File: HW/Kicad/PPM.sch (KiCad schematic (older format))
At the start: 400 parts, among them J1 12V, J10 hole, J11 hole, J12 hole, J13 hole, J14 External GPIOs, J15 External GPIOs, J16 External GPIOs, J17 C ext, J18 TP, J19 Shield pad, J2 PPM_sensor, J20 TP, J21 Shield pad, J22 TP, J23 Shield pad, J24 Shield pad, J25 Shield pad, J26 Shield pad, J27 Shield pad, J28 Shield pad, J29 Shield pad, J3 RS232, J30 Shield pad, J4 USB_B, J5 UART5, J6 SWD, J7 External GPIOs, J8 UART1, J9 Batt, Q1 DMPH4015SSSQ-13, Q10 IRF740, Q11 BC847, Q12 BC847, Q13 BC847, Q14 BC847, Q15 BC847, Q16 BC847, Q17 BC847, Q18 BC847, Q2 ZTX851, Q3 ZTX851, Q4 IRF9640, Q5 BC847, Q6 IRF740, Q7 IRF740, Q8 IRF640, Q9 IRF740, T1 Filter, T2 78253_55JC, U1 TPS7A4700, U10 LT1677, U11 STM32F767VITx, U12 LT1677, U13 MAX6043, U14 MAX11100, U15 ADCMP609, U16 LTC6655, U17 LT1677, U18 MCP1501-30E_SN, U19 LT1677, U2 LT1677, U20 MCP6021, U21 SN74ACT244-Q1, U22 MAX3227EE, U23 FT230XS, U24 ADuM226N, U25 SN6505, U3 ADA4841-1YRJ, U4 ADA4841-1YRJ, U5 ADA4841-1YRJ, U6 ADA4841-1YRJ, U7 XTCLH, U8 TL1963A-33KTTR, U9 LT1777, Y1 32.768kHz

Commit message: fixed bugs in schema
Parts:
- removed C70: 22u, Mylib_Footprints:C1206, symbol Device:C
- removed R55: 47k, Mylib_Footprints:R0805, symbol Device:R
- added R?: 10, Mylib_Footprints:R0805, symbol Device:R
- R54: value 47 -> 680k
- U20: value MCP6021 -> MCP6021R
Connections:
- net 3V_ref: now also R?.2; no longer C94.1, U18.7 (OUT), U18.8 (FB)
- net GNDA: now also Q6.3 (S); no longer Q6.2 (D)
- net at J2.1 (Pin_1), Q4.2 (D): now also Q6.2 (D); no longer Q6.3 (S)
- net at JP14.1, U10.6: now also C68.1, R51.2
- new net: C94.1, R?.1, U18.7 (OUT), U18.8 (FB)
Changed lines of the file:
@@
 	0    1    1    0
 $EndComp
-Connection ~ 12100 4950
 Wire Wire Line
 	10500 5300 10500 5350
@@
 	10150 4500 10150 4550
 Wire Wire Line
-	12100 6000 12100 5650
-$Comp
-L PPM-rescue:GNDA-MyLib-Power_Symbols #PWR0140
-U 1 1 622B4B6D
-P 12100 6000
-F 0 "#PWR0140" H 12100 5750 50  0001 C CNN
-F 1 "GNDA" H 12100 5850 50  0000 C CNN
-F 2 "" H 12100 6000 50  0001 C CNN
-F 3 "" H 12100 6000 50  0001 C CNN
-	1    12100 6000
-	1    0    0    -1
-$EndComp
-Wire Wire Line
-	12100 4950 12100 5350
-Wire Wire Line
-	11800 4950 12100 4950
-$Comp
-L Device:R R55
-U 1 1 622A01CE
-P 12100 5500
-F 0 "R55" H 12170 5546 50  0000 L CNN
-F 1 "47k" H 12170 5455 50  0000 L CNN
-F 2 "Mylib_Footprints:R0805" V 12030 5500 50  0001 C CNN
-F 3 "~" H 12100 5500 50  0001 C CNN
-	1    12100 5500
-	1    0    0    -1
-$EndComp
-Wire Wire Line
 	10500 4950 10500 5000
 Connection ~ 10500 4950
 Wire Wire Line
-	10500 4950 11500 4950
-$Comp
-L Device:C C70
-U 1 1 6223C12C
-P 11650 4950
-F 0 "C70" V 11600 5000 50  0000 L CNN
-F 1 "22u" V 11700 5000 50  0000 L CNN
-F 2 "Mylib_Footprints:C1206" H 11688 4800 50  0001 C CNN
-F 3 "~" H 11650 4950 50  0001 C CNN
-	1    11650 4950
-	0    1    1    0
-$EndComp
-Wire Wire Line
 	10500 4900 10500 4950
 Connection ~ 10500 5350
@@
 P 16050 7550
 F 0 "U20" H 16000 7700 50  0000 L CNN
-F 1 "MCP6021" H 16000 7400 50  0000 L CNN
+F 1 "MCP6021R" H 16000 7400 50  0000 L CNN
 F 2 "Package_TO_SOT_SMD:SOT-23-5" H 16050 7550 50  0001 C CNN
 F 3 "~" H 16050 7550 50  0001 C CNN
@@
 P 16100 5450
 F 0 "R54" H 16170 5496 50  0000 L CNN
-F 1 "47" H 16170 5405 50  0000 L CNN
+F 1 "680k" H 16170 5405 50  0000 L CNN
 F 2 "Mylib_Footprints:R0805" V 16030 5450 50  0001 C CNN
 F 3 "~" H 16100 5450 50  0001 C CNN
@@
 Wire Wire Line
 	1250 6200 1250 6150
-Text GLabel 2700 5800 2    50   Input ~ 0
+Text GLabel 3000 5800 2    50   Input ~ 0
 3V_ref
 Wire Wire Line
@@
 F 3 "~" H 2350 8550 50  0001 C CNN
 	1    2350 8550
-	-1   0    0    1
+	-1   0    0    -1
 $EndComp
 $Comp
@@
 	1    0    0    1
 $EndComp
+$Comp
+L Device:R R?
+U 1 1 6097F89E
+P 2850 5800
+F 0 "R?" V 2950 5750 50  0000 L CNN
+F 1 "10" V 2750 5750 50  0000 L CNN
+F 2 "Mylib_Footprints:R0805" V 2780 5800 50  0001 C CNN
+F 3 "~" H 2850 5800 50  0001 C CNN
+	1    2850 5800
+	0    -1   -1   0
+$EndComp
+Wire Wire Line
+	10500 4950 12100 4950
 $EndSCHEMATC

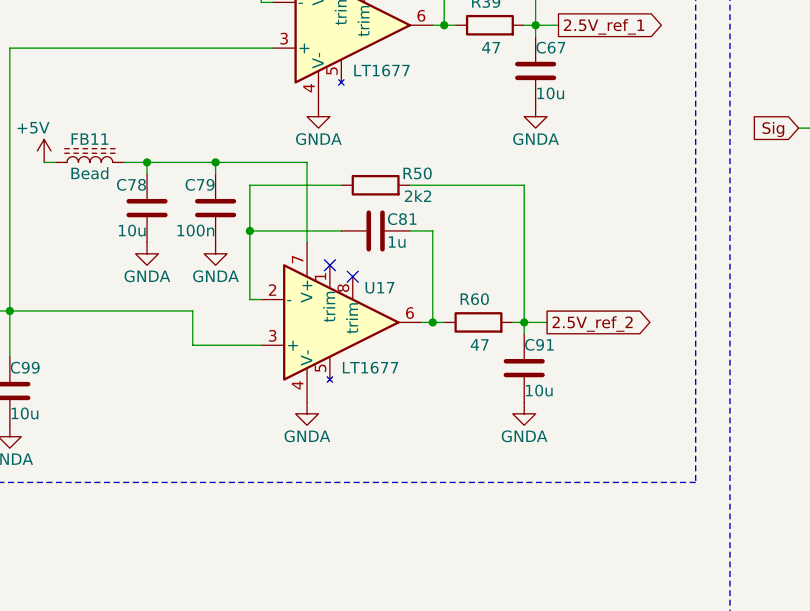
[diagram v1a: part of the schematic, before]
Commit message: changed TIM5 period to 50 us
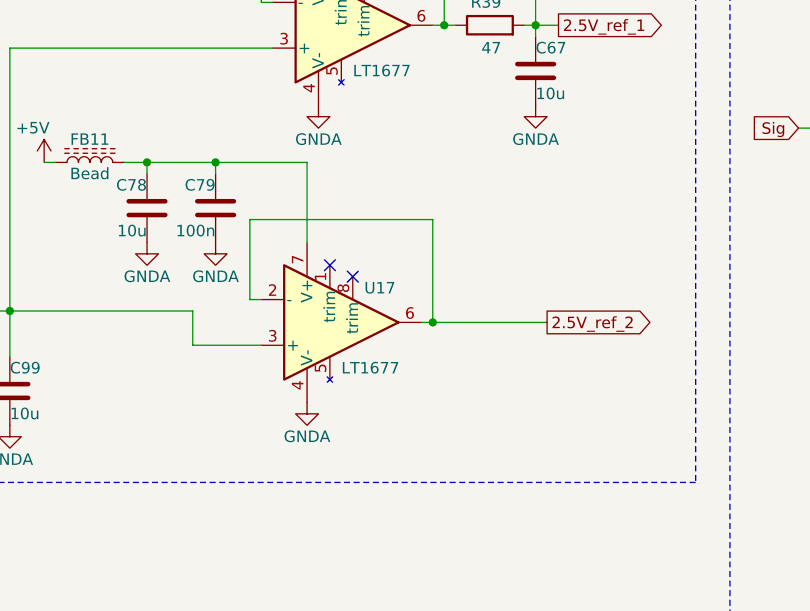
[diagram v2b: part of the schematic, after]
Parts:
- removed C81: 1u, Mylib_Footprints:C0805, symbol Device:C
- removed C91: 10u, Mylib_Footprints:C1206, symbol Device:C
- removed R50: 2k2, Mylib_Footprints:R0805, symbol Device:R
- removed R60: 47, Mylib_Footprints:R0805, symbol Device:R
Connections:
- net 2.5V_ref_2: now also U17.2 (-), U17.6
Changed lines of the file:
@@
 Text GLabel 7950 5750 2    50   Output ~ 0
 2.5V_ref_2
-$Comp
-L Device:R R50
-U 1 1 63857DA7
-P 7200 5150
-F 0 "R50" V 7250 4900 50  0000 L CNN
-F 1 "2k2" V 7150 4900 50  0000 L CNN
-F 2 "Mylib_Footprints:R0805" V 7130 5150 50  0001 C CNN
-F 3 "~" H 7200 5150 50  0001 C CNN
-	1    7200 5150
-	0    -1   -1   0
-$EndComp
 Wire Wire Line
 	6900 5050 6900 5400
@@
 NoConn ~ 7000 5500
 NoConn ~ 7100 5550
-$Comp
-L Device:C C81
-U 1 1 63857D66
-P 7200 5350
-F 0 "C81" V 7150 5400 50  0000 L CNN
-F 1 "1u" V 7250 5400 50  0000 L CNN
-F 2 "Mylib_Footprints:C0805" H 7238 5200 50  0001 C CNN
-F 3 "~" H 7200 5350 50  0001 C CNN
-	1    7200 5350
-	0    1    1    0
-$EndComp
-$Comp
-L Device:R R60
-U 1 1 63857D60
-P 7650 5750
-F 0 "R60" V 7750 5700 50  0000 L CNN
-F 1 "47" V 7550 5700 50  0000 L CNN
-F 2 "Mylib_Footprints:R0805" V 7580 5750 50  0001 C CNN
-F 3 "~" H 7650 5750 50  0001 C CNN
-	1    7650 5750
-	0    -1   -1   0
-$EndComp
-$Comp
-L Device:C C91
-U 1 1 63857D5A
-P 7850 5950
-F 0 "C91" H 7850 6050 50  0000 L CNN
-F 1 "10u" H 7850 5850 50  0000 L CNN
-F 2 "Mylib_Footprints:C1206" H 7888 5800 50  0001 C CNN
-F 3 "~" H 7850 5950 50  0001 C CNN
-	1    7850 5950
-	1    0    0    -1
-$EndComp
-Wire Wire Line
-	7500 5750 7450 5750
-Wire Wire Line
-	7800 5750 7850 5750
-Wire Wire Line
-	7850 5750 7850 5800
-Wire Wire Line
-	7350 5350 7450 5350
-Wire Wire Line
-	7450 5350 7450 5750
+Wire Wire Line
+	7450 5300 7450 5750
 Connection ~ 7450 5750
 Wire Wire Line
 	7450 5750 7400 5750
 Wire Wire Line
-	7050 5350 6650 5350
-Wire Wire Line
-	6650 5350 6650 5650
+	6650 5300 6650 5650
 Wire Wire Line
 	6650 5650 6700 5650
-Wire Wire Line
-	7050 5150 6650 5150
-Wire Wire Line
-	6650 5150 6650 5350
-Connection ~ 6650 5350
-Wire Wire Line
-	7850 5150 7850 5750
-Wire Wire Line
-	7350 5150 7850 5150
-Connection ~ 7850 5750
-$Comp
-L PPM-rescue:GNDA-MyLib-Power_Symbols #PWR0142
-U 1 1 63857D44
-P 7850 6100
-F 0 "#PWR0142" H 7850 5850 50  0001 C CNN
-F 1 "GNDA" H 7850 5950 50  0000 C CNN
-F 2 "" H 7850 6100 50  0001 C CNN
-F 3 "" H 7850 6100 50  0001 C CNN
-	1    7850 6100
-	1    0    0    -1
-$EndComp
-Wire Wire Line
-	7850 5750 7950 5750
 Wire Wire Line
 	5600 4550 5600 5700
@@
 Wire Wire Line
 	10500 4950 12100 4950
+Wire Wire Line
+	6650 5300 7450 5300
+Wire Wire Line
+	7450 5750 7950 5750
 $EndSCHEMATC

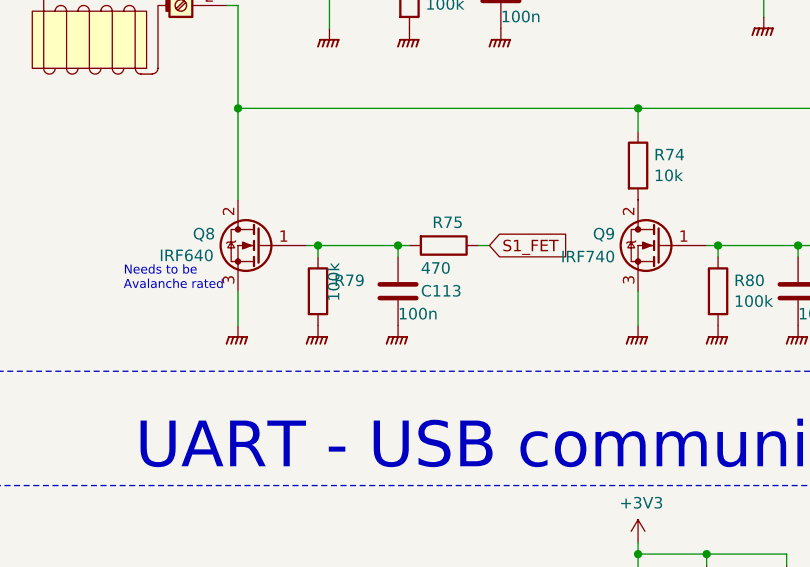
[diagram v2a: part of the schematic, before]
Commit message: added script to plot measured data from oscilloscope and fixed bug with SPI
bugfix:
boosted priority of DMA2 for SPI communication in order to fix problems with busy wait after RX. It seems that when he priority was low, than sometimes the settings for DMA wasn't fast enough and than it missed some data
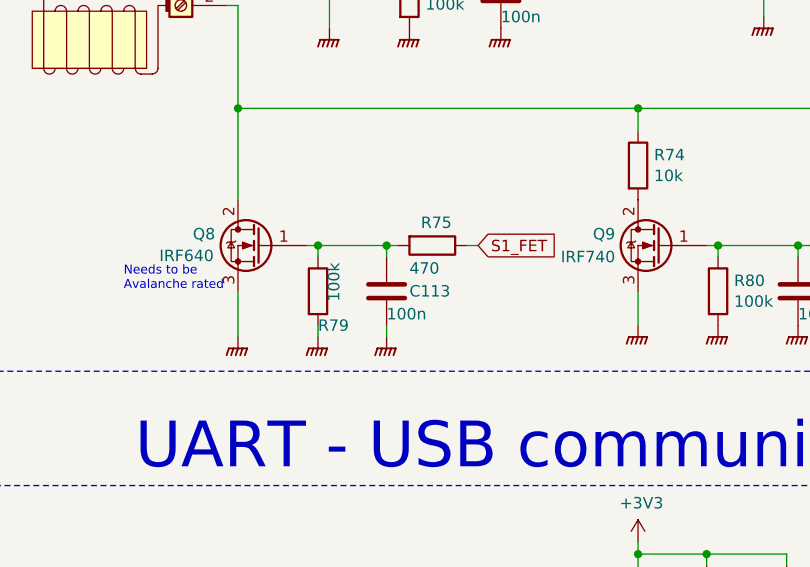
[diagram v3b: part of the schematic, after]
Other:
- moved on the sheet: C113, R75
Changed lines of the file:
@@
 L PPM-rescue:GNDPWR-MyLib-Power_Symbols #PWR0181
 U 1 1 61985062
-P 1850 10200
-F 0 "#PWR0181" H 1850 9950 50  0001 C CNN
-F 1 "GNDPWR" H 1850 10050 50  0001 C CNN
-F 2 "" H 1850 10200 50  0001 C CNN
-F 3 "" H 1850 10200 50  0001 C CNN
-	1    1850 10200
+P 1850 10250
+F 0 "#PWR0181" H 1850 10000 50  0001 C CNN
+F 1 "GNDPWR" H 1850 10100 50  0001 C CNN
+F 2 "" H 1850 10250 50  0001 C CNN
+F 3 "" H 1850 10250 50  0001 C CNN
+	1    1850 10250
 	1    0    0    -1
 $EndComp
 Wire Wire Line
-	1850 10200 1850 10050
+	1850 10250 1850 10050
 $Comp
 L PPM-rescue:GNDPWR-MyLib-Power_Symbols #PWR0184
@@
 U 1 1 61C83792
 P 2200 10050
-F 0 "R79" H 2270 10096 50  0000 L CNN
+F 0 "R79" H 2200 9900 50  0000 L CNN
 F 1 "100k" V 2270 10005 50  0000 L CNN
 F 2 "Mylib_Footprints:R0805" V 2130 10050 50  0001 C CNN
@@
 L PPM-rescue:GNDPWR-MyLib-Power_Symbols #PWR0182
 U 1 1 61C8379A
-P 2200 10200
-F 0 "#PWR0182" H 2200 9950 50  0001 C CNN
-F 1 "GNDPWR" H 2200 10050 50  0001 C CNN
-F 2 "" H 2200 10200 50  0001 C CNN
-F 3 "" H 2200 10200 50  0001 C CNN
-	1    2200 10200
+P 2200 10250
+F 0 "#PWR0182" H 2200 10000 50  0001 C CNN
+F 1 "GNDPWR" H 2200 10100 50  0001 C CNN
+F 2 "" H 2200 10250 50  0001 C CNN
+F 3 "" H 2200 10250 50  0001 C CNN
+	1    2200 10250
 	1    0    0    -1
 $EndComp
@@
 L Device:C C113
 U 1 1 60286EBF
-P 2550 10050
-F 0 "C113" H 2650 10050 50  0000 L CNN
-F 1 "100n" H 2550 9950 50  0000 L CNN
-F 2 "Mylib_Footprints:C0805" H 2588 9900 50  0001 C CNN
-F 3 "~" H 2550 10050 50  0001 C CNN
-	1    2550 10050
+P 2500 10050
+F 0 "C113" H 2600 10050 50  0000 L CNN
+F 1 "100n" H 2500 9950 50  0000 L CNN
+F 2 "Mylib_Footprints:C0805" H 2538 9900 50  0001 C CNN
+F 3 "~" H 2500 10050 50  0001 C CNN
+	1    2500 10050
 	1    0    0    -1
 $EndComp
@@
 L Device:R R75
 U 1 1 60286EC5
-P 2750 9850
-F 0 "R75" V 2650 9800 50  0000 L CNN
-F 1 "470" V 2850 9750 50  0000 L CNN
-F 2 "Mylib_Footprints:R0805" V 2680 9850 50  0001 C CNN
-F 3 "~" H 2750 9850 50  0001 C CNN
-	1    2750 9850
+P 2700 9850
+F 0 "R75" V 2600 9800 50  0000 L CNN
+F 1 "470" V 2800 9750 50  0000 L CNN
+F 2 "Mylib_Footprints:R0805" V 2630 9850 50  0001 C CNN
+F 3 "~" H 2700 9850 50  0001 C CNN
+	1    2700 9850
 	0    1    1    0
 $EndComp
 Wire Wire Line
-	2600 9850 2550 9850
+	2550 9850 2500 9850
 Wire Wire Line
-	2550 9850 2550 9900
-Connection ~ 2550 9850
+	2500 9850 2500 9900
+Connection ~ 2500 9850
 $Comp
 L PPM-rescue:GNDPWR-MyLib-Power_Symbols #PWR0183
 U 1 1 60286ECE
-P 2550 10200
-F 0 "#PWR0183" H 2550 9950 50  0001 C CNN
-F 1 "GNDPWR" H 2550 10050 50  0001 C CNN
-F 2 "" H 2550 10200 50  0001 C CNN
-F 3 "" H 2550 10200 50  0001 C CNN
-	1    2550 10200
+P 2500 10250
+F 0 "#PWR0183" H 2500 10000 50  0001 C CNN
+F 1 "GNDPWR" H 2500 10100 50  0001 C CNN
+F 2 "" H 2500 10250 50  0001 C CNN
+F 3 "" H 2500 10250 50  0001 C CNN
+	1    2500 10250
 	1    0    0    -1
 $EndComp
 Wire Wire Line
-	2950 9850 2900 9850
+	2900 9850 2850 9850
 Wire Wire Line
-	2200 9850 2550 9850
+	2200 9850 2500 9850
 Wire Notes Line
 	800  7050 8300 7050
@@
 Text GLabel 5650 9850 2    50   Input ~ 0
 S2_FET
-Text GLabel 2950 9850 2    50   Input ~ 0
+Text GLabel 2900 9850 2    50   Input ~ 0
 S1_FET
 $Comp
@@
 Wire Wire Line
 	7450 5750 7950 5750
+Wire Wire Line
+	2500 10250 2500 10200
+Wire Wire Line
+	2200 10250 2200 10200
 $EndSCHEMATC

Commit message: The device was constructed and finally bring to live
There were some mistakes that are now fixed in schema, but still wrong on PCB. Keep it in mind...
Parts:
- removed C115, C116: 100n, Mylib_Footprints:C0805, symbol Device:C
- removed Q10, Q7: IRF740, Package_TO_SOT_THT:TO-220-3_Vertical, symbol Device:Q_NMOS_GDS
- removed R73, R81: 100k, Mylib_Footprints:R0805, symbol Device:R
- removed R77, R78: 470, Mylib_Footprints:R0805, symbol Device:R
- added D?: D, symbol Device:D
- added K?: DIPxx-1Cxx-51x, Relay_THT:Relay_StandexMeder_DIP_LowProfile, symbol Relay:DIPxx-1Cxx-51x
- added Q?: BC847, Package_TO_SOT_SMD:SOT-23, symbol Transistor_BJT:BC847
- added R?: 4k7, Mylib_Footprints:R0805, symbol Device:R
- added R?: 20, Mylib_Footprints:R0805, symbol Device:R
- C13: value 100u tantal -> 100u
- D2: value D_TVS -> Transil/27V
- J1: value 12V -> 12V - 24V
- RV1: value Varistor -> Varistor/27V
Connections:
- net +6V: now also R?.2
- net GNDA: now also K?.1, Q?.2 (E)
- net S3_FET: now also R?.2
- net Sig: now also K?.7, K?.8
- net at J2.2 (Pin_2), Q8.2 (D), R74.1: now also K?.14
- new net: Q?.1 (B), R?.1
- new net: D?.2 (A), K?.2, Q?.3 (C)
- new net: D?.1 (K), K?.6, R?.1
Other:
- note added: "R = 104"
- moved on the sheet: C11, C12, C120, C121, C122, C123, C124, C125, C126, C127, C128, C129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

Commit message: firmware code was split from main to dedicated files to make the code more readable
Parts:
- added J?: Control signals, Connector_PinHeader_2.54mm:PinHeader_1x05_P2.54mm_Vertical, symbol Connector:Screw_Terminal_01x07
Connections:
- net GNDA: now also J?.1 (Pin_1)
- net S1_FET: now also J?.7 (Pin_7)
- net S2_FET: now also J?.6 (Pin_6)
- net S3_FET: now also J?.5 (Pin_5)
- net S4_FET: now also J?.4 (Pin_4)
- net S5_FET: now also J?.3 (Pin_3)
- net S6_FET: now also J?.2 (Pin_2)
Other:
- note added: "problems due to ground loops"
- moved on the sheet: C106, C107, C111, C112, C113, C114, C137, C73, C74, C92, C93, C94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
